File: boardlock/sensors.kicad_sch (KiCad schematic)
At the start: 16 parts, among them Q2 Q_NPN_BCE, Q3 Q_NPN_BCE, Q4 BSS84PWH6327XTSA1, U1 LSM6DSO32, U3 SAM-M8Q

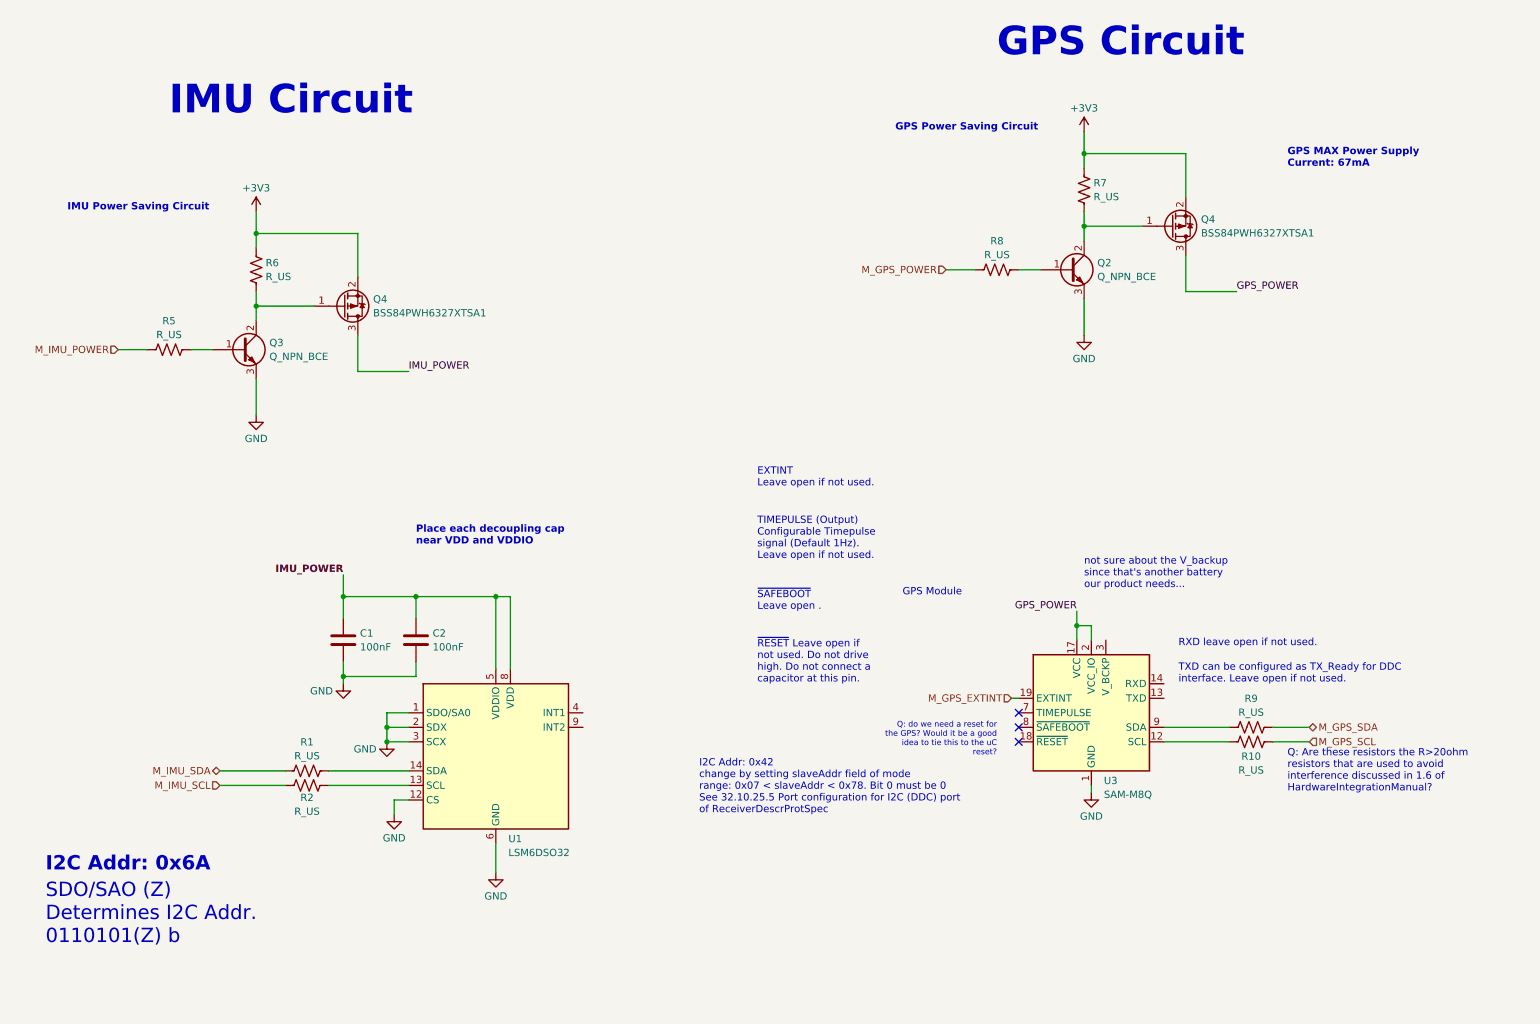
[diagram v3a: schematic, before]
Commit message: Added power library and fixed labels
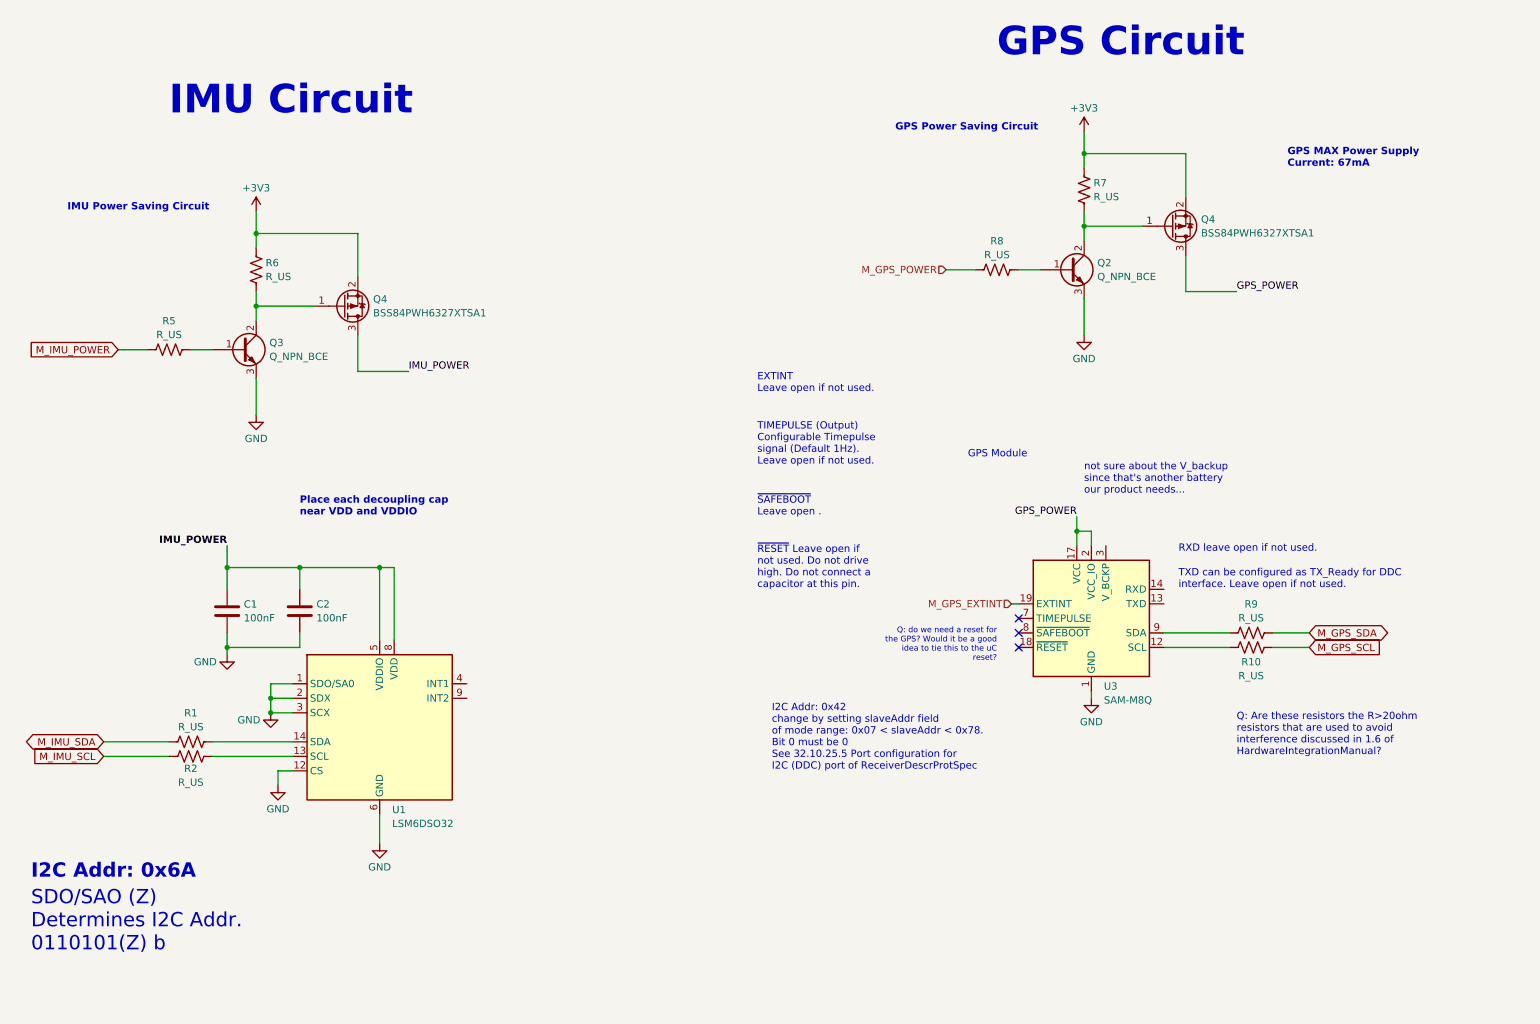
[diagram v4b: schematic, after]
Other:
- moved on the sheet: C1, C2, R1, R10, R2, R9, U1, U3

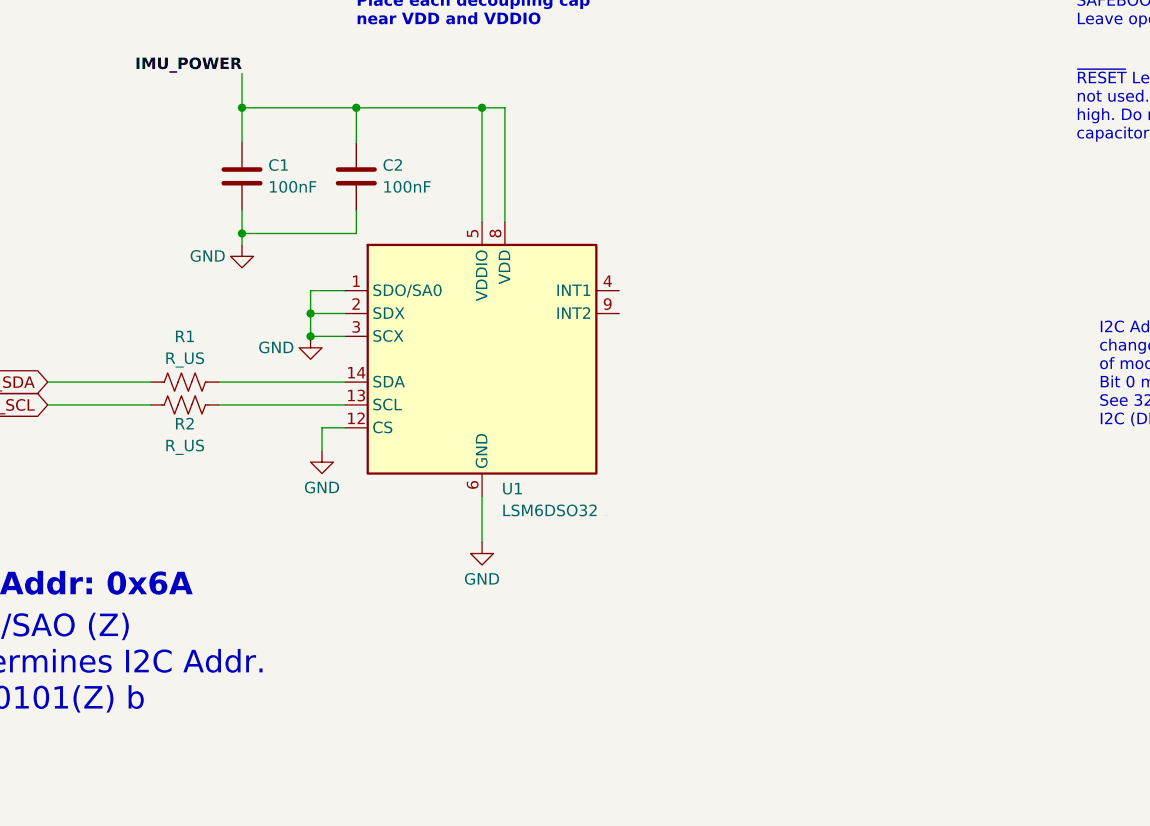
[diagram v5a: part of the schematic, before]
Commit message: sensor wire modifications
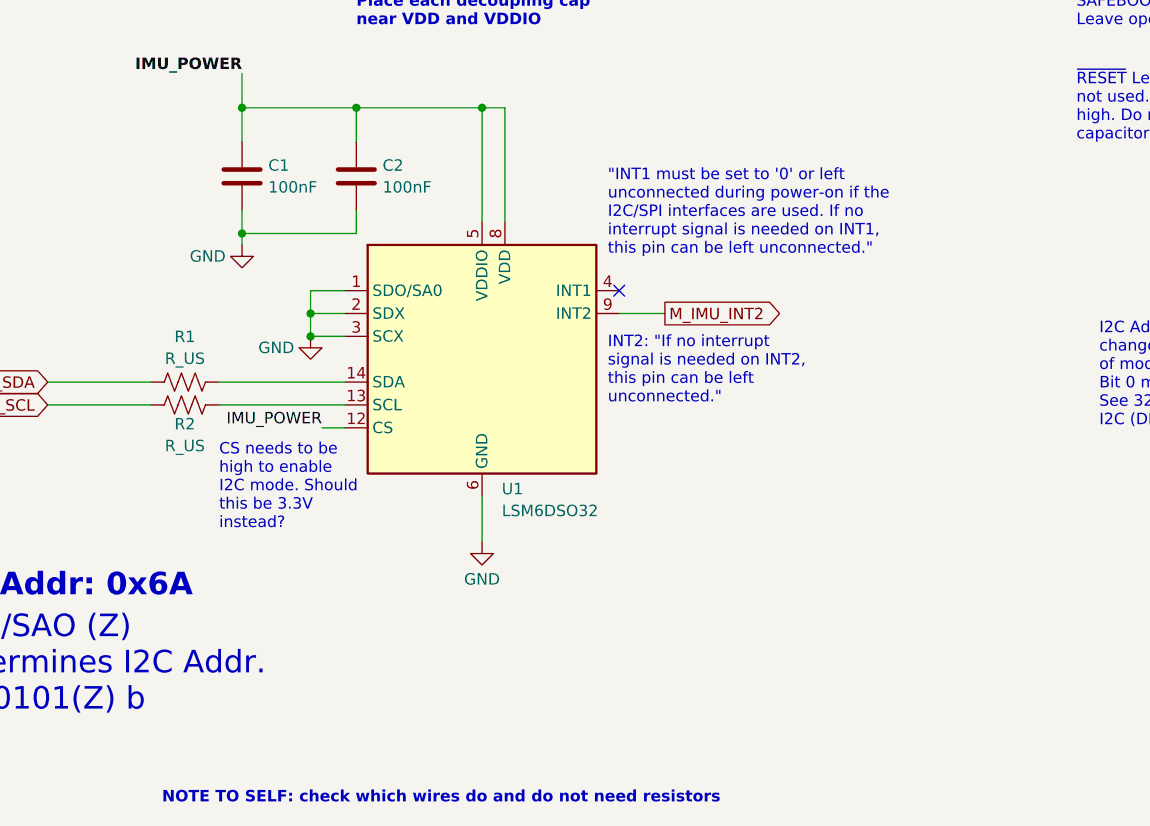
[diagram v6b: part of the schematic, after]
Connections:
- net GND: no longer U1.12 (CS)
- net IMU_POWER: now also U1.12 (CS)
- net M_IMU_INT2: now reaches U1.9 (INT2)
- no-connect marks 3 -> 4
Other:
- note added: ""INT1 must be set to '0' or left unconnected during power-on if the I2C/SPI interfaces are used. If no interrupt signal is needed on INT1, this pin can be left unconnected.""
- note added: "CS needs to be high to enable I2C mode. Should this be 3.3V instead?"
- note added: "INT2: "If no interrupt signal is needed on INT2, this pin can be left unconnected.""
- note added: "NOTE TO SELF: check which wires do and do not need resistors"
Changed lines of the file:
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@@
   (no_connect (at 200.66 124.46))
   (no_connect (at 200.66 119.38))
+  (no_connect (at 104.14 130.81))
   (wire (pts (xy 199.39 116.84) (xy 200.66 116.84))
     (stroke (width 0) (type default))
@@
     (stroke (width 0) (type default))
   )
+  (wire (pts (xy 85.09 69.85) (xy 85.09 76.2))
+    (stroke (width 0) (type default))
+  )
+  (wire (pts (xy 62.23 110.49) (xy 74.93 110.49))
+    (stroke (width 0) (type default))
+  )
+  (wire (pts (xy 59.69 140.97) (xy 73.66 140.97))
+    (stroke (width 0) (type default))
+  )
+  (wire (pts (xy 67.31 77.47) (xy 67.31 83.82))
+    (stroke (width 0) (type default))
+  )
+  (wire (pts (xy 210.82 104.14) (xy 213.36 104.14))
+    (stroke (width 0) (type default))
+  )
+  (wire (pts (xy 226.06 121.92) (xy 237.49 121.92))
+    (stroke (width 0) (type default))
+  )
+  (wire (pts (xy 69.85 133.35) (xy 69.85 135.89))
+    (stroke (width 0) (type default))
+  )
+  (wire (pts (xy 245.11 124.46) (xy 251.46 124.46))
+    (stroke (width 0) (type default))
+  )
+  (wire (pts (xy 213.36 104.14) (xy 213.36 106.68))
+    (stroke (width 0) (type default))
+  )
+  (wire (pts (xy 62.23 124.46) (xy 62.23 125.73))
+    (stroke (width 0) (type default))
+  )
+  (wire (pts (xy 229.87 38.1) (xy 229.87 45.72))
+    (stroke (width 0) (type default))
+  )
+  (wire (pts (xy 77.47 64.77) (xy 67.31 64.77))
+    (stroke (width 0) (type default))
+  )
+  (wire (pts (xy 40.64 143.51) (xy 52.07 143.51))
+    (stroke (width 0) (type default))
+  )
+  (wire (pts (xy 88.9 110.49) (xy 91.44 110.49))
+    (stroke (width 0) (type default))
+  )
+  (wire (pts (xy 212.09 34.29) (xy 212.09 38.1))
+    (stroke (width 0) (type default))
+  )
+  (wire (pts (xy 229.87 55.88) (xy 229.87 62.23))
+    (stroke (width 0) (type default))
+  )
+  (wire (pts (xy 67.31 62.23) (xy 67.31 64.77))
+    (stroke (width 0) (type default))
+  )
   (wire (pts (xy 71.12 146.05) (xy 73.66 146.05))
     (stroke (width 0) (type default))
   )
-  (wire (pts (xy 85.09 69.85) (xy 85.09 76.2))
-    (stroke (width 0) (type default))
-  )
-  (wire (pts (xy 62.23 110.49) (xy 74.93 110.49))
-    (stroke (width 0) (type default))
-  )
-  (wire (pts (xy 59.69 140.97) (xy 73.66 140.97))
-    (stroke (width 0) (type default))
-  )
-  (wire (pts (xy 67.31 77.47) (xy 67.31 83.82))
-    (stroke (width 0) (type default))
-  )
-  (wire (pts (xy 210.82 104.14) (xy 213.36 104.14))
-    (stroke (width 0) (type default))
-  )
-  (wire (pts (xy 226.06 121.92) (xy 237.49 121.92))
-    (stroke (width 0) (type default))
-  )
-  (wire (pts (xy 69.85 133.35) (xy 69.85 135.89))
-    (stroke (width 0) (type default))
-  )
-  (wire (pts (xy 245.11 124.46) (xy 251.46 124.46))
-    (stroke (width 0) (type default))
-  )
-  (wire (pts (xy 213.36 104.14) (xy 213.36 106.68))
-    (stroke (width 0) (type default))
-  )
-  (wire (pts (xy 62.23 124.46) (xy 62.23 125.73))
-    (stroke (width 0) (type default))
-  )
-  (wire (pts (xy 229.87 38.1) (xy 229.87 45.72))
-    (stroke (width 0) (type default))
-  )
-  (wire (pts (xy 77.47 64.77) (xy 67.31 64.77))
-    (stroke (width 0) (type default))
-  )
-  (wire (pts (xy 40.64 143.51) (xy 52.07 143.51))
-    (stroke (width 0) (type default))
-  )
-  (wire (pts (xy 88.9 110.49) (xy 91.44 110.49))
-    (stroke (width 0) (type default))
-  )
-  (wire (pts (xy 212.09 34.29) (xy 212.09 38.1))
-    (stroke (width 0) (type default))
-  )
-  (wire (pts (xy 229.87 55.88) (xy 229.87 62.23))
-    (stroke (width 0) (type default))
-  )
-  (wire (pts (xy 67.31 62.23) (xy 67.31 64.77))
-    (stroke (width 0) (type default))
-  )
   (wire (pts (xy 85.09 52.07) (xy 85.09 59.69))
     (stroke (width 0) (type default))
@@
     (stroke (width 0) (type default))
   )
-  (wire (pts (xy 71.12 148.59) (xy 71.12 146.05))
-    (stroke (width 0) (type default))
-  )
   (wire (pts (xy 229.87 62.23) (xy 238.76 62.23))
     (stroke (width 0) (type default))
@@
   )
   (wire (pts (xy 67.31 52.07) (xy 85.09 52.07))
+    (stroke (width 0) (type default))
+  )
+  (wire (pts (xy 104.14 133.35) (xy 109.22 133.35))
     (stroke (width 0) (type default))
   )
@@
     (effects (font (size 1.27 1.27) bold) (justify left bottom))
   )
+  (text "INT2: \"If no interrupt \nsignal is needed on INT2, \nthis pin can be left \nunconnected.\""
+    (at 102.87 143.51 0)
+    (effects (font (size 1.27 1.27)) (justify left bottom))
+  )
   (text "not sure about the V_backup \nsince that's another battery \nour product needs..."
     (at 212.09 97.79 0)
@@
     (effects (font (size 2.5 2.5)) (justify left bottom))
   )
+  (text "NOTE TO SELF: check which wires do and do not need resistors\n"
+    (at 53.34 187.96 0)
+    (effects (font (size 1.27 1.27) (thickness 0.254) bold) (justify left bottom))
+  )
   (text "TXD can be configured as TX_Ready for DDC \ninterface. Leave open if not used.\n"
     (at 228.6 114.3 0)
     (effects (font (size 1.27 1.27)) (justify left bottom))
   )
+  (text "\"INT1 must be set to '0' or left \nunconnected during power-on if the \nI2C/SPI interfaces are used. If no \ninterrupt signal is needed on INT1, \nthis pin can be left unconnected.\""
+    (at 102.87 127 0)
+    (effects (font (size 1.27 1.27)) (justify left bottom))
+  )
   (text "RXD leave open if not used." (at 228.6 107.95 0)
     (effects (font (size 1.27 1.27)) (justify left bottom))
+  )
+  (text "CS needs to be \nhigh to enable \nI2C mode. Should \nthis be 3.3V \ninstead?"
+    (at 59.69 157.48 0)
+    (effects (font (size 1.27 1.27)) (justify left bottom))
+  )
+  (label "IMU_POWER" (at 71.12 146.05 180) (fields_autoplaced)
+    (effects (font (size 1.27 1.27)) (justify right bottom))
   )
   (label "IMU_POWER" (at 93.98 76.2 0) (fields_autoplaced)
@@
   (label "GPS_POWER" (at 210.82 101.6 180) (fields_autoplaced)
     (effects (font (size 1.27 1.27)) (justify right bottom))
+  )
+  (global_label "M_IMU_INT2" (shape output) (at 109.22 133.35 0) (fields_autoplaced)
+    (effects (font (size 1.27 1.27)) (justify left))
+    (property "Intersheetrefs" "${INTERSHEET_REFS}" (at 123.0909 133.35 0)
+      (effects (font (size 1.27 1.27)) (justify left) hide)
+    )
   )
   (global_label "M_IMU_SCL" (shape input) (at 40.64 143.51 180) (fields_autoplaced)
@@
         )
       )
-    )
-  )
-  (symbol (lib_id "power:GND") (at 71.12 148.59 0) (unit 1)
-    (in_bom yes) (on_board yes) (dnp no) (fields_autoplaced)
-    (property "Reference" "#PWR08" (at 71.12 154.94 0)
-      (effects (font (size 1.27 1.27)) hide)
-    )
-    (property "Value" "GND" (at 71.12 152.7231 0)
-      (effects (font (size 1.27 1.27)))
-    )
-    (property "Footprint" "" (at 71.12 148.59 0)
-      (effects (font (size 1.27 1.27)) hide)
-    )
-    (property "Datasheet" "" (at 71.12 148.59 0)
-      (effects (font (size 1.27 1.27)) hide)
-    )
-    (pin "1")
-    (instances
-      (project "boardlock"
-        (path "/48f24f42-fd64-4860-9f12-ca34cf195758/17b4aebf-aea4-4bb2-a07c-86de8cf47820"
-          (reference "#PWR08") (unit 1)
-        )
-        (path "/48f24f42-fd64-4860-9f12-ca34cf195758/17b4aebf-aea4-4bb2-a07c-86de8cf47820/50767468-7b8a-48f0-9e61-53ec0e447e69"
-          (reference "#PWR08") (unit 1)
-        )
-      )
-      (project "boardlock"
-        (path "/e1fc29ce-837e-4062-84d8-c7e423f9eab9/a4a6f965-a4d9-4da6-b64e-79eda0daabe5"
-          (reference "#PWR08") (unit 1)
-        )
-      )
